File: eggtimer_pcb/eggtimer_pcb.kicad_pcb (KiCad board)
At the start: 2 copper layers, 71.1 x 71.1 mm, 112 parts, among them J1 Conn_01x03, Q1 CPH3350-TL-W, Q10 2N7002P,215, Q11 CPH3350-TL-W, Q12 CPH3350-TL-W, Q2 CPH3350-TL-W, Q3 CPH3350-TL-W, Q4 CPH3350-TL-W, Q5 CPH3350-TL-W, Q6 CPH3350-TL-W, Q7 CPH3350-TL-W, Q8 CPH3350-TL-W, Q9 2N7002P,215, SW1 Rotary_Encoder_Switch, SW2 SW_Push, U1 BD70522GUL-E2, U2 STM32G051GxU, Y1 32.xxxk

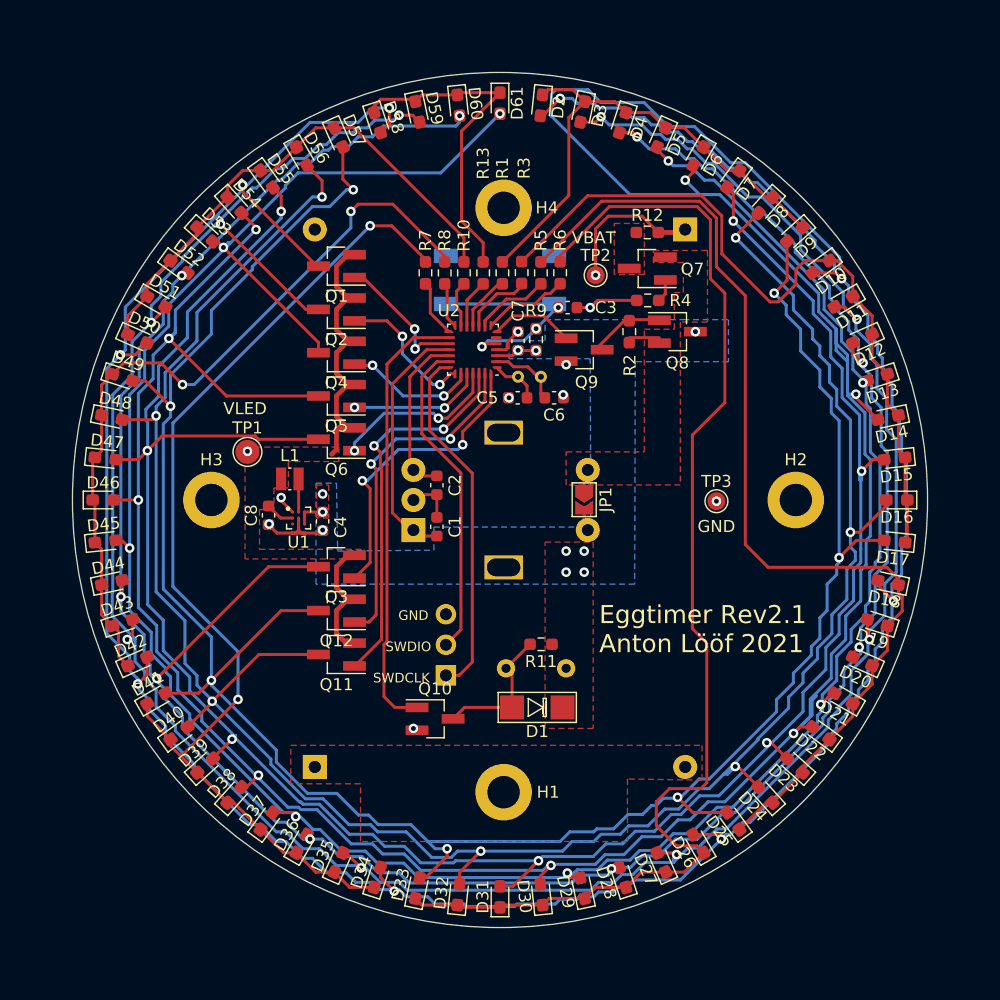
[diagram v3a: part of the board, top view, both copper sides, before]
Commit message: fix some distances
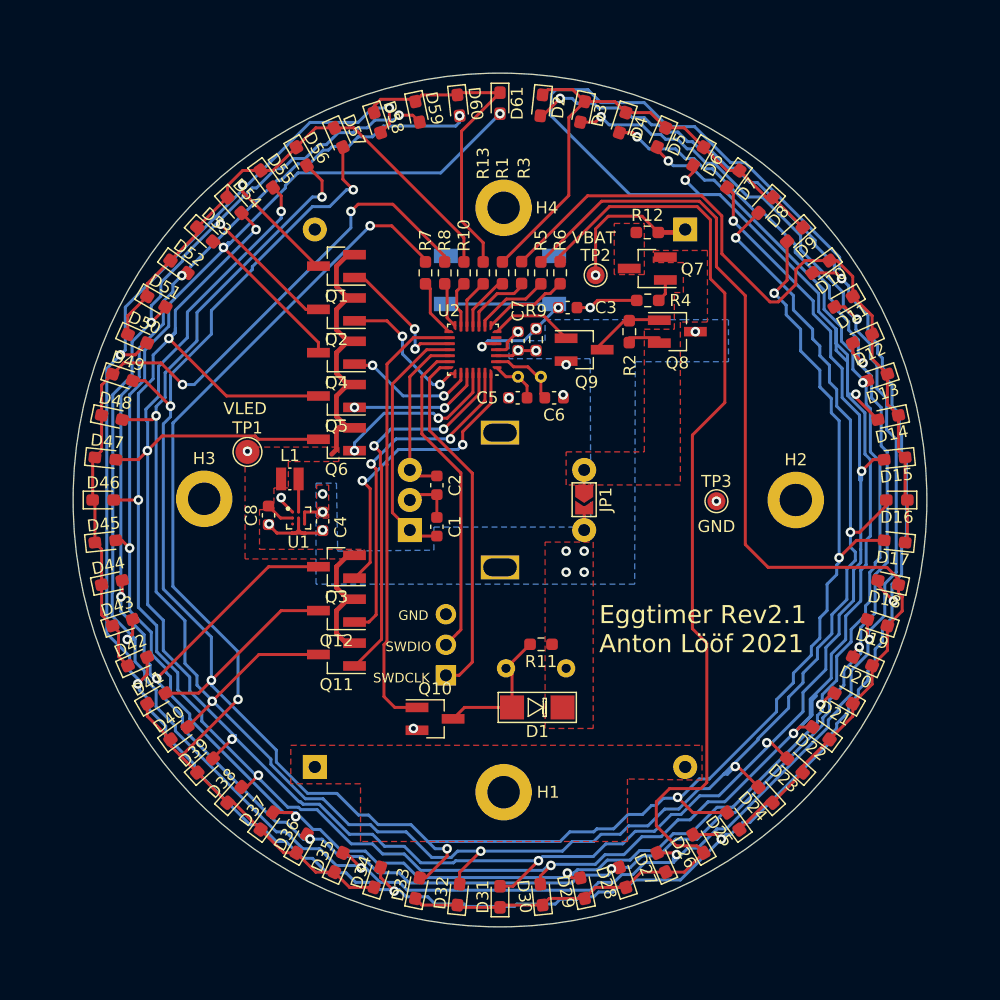
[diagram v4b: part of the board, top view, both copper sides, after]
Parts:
- moved H3 0.61 mm to (116.4, 115.9)
- moved SW1 0.30 mm to (133.5, 118.5)
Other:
- board size 71.1 x 71.1 mm -> 71 x 71 mm

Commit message: Use kicad6
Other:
- net class Default removed
